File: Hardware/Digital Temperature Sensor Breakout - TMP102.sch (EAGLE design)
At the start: 12 parts, among them U1 TMP102-1:1

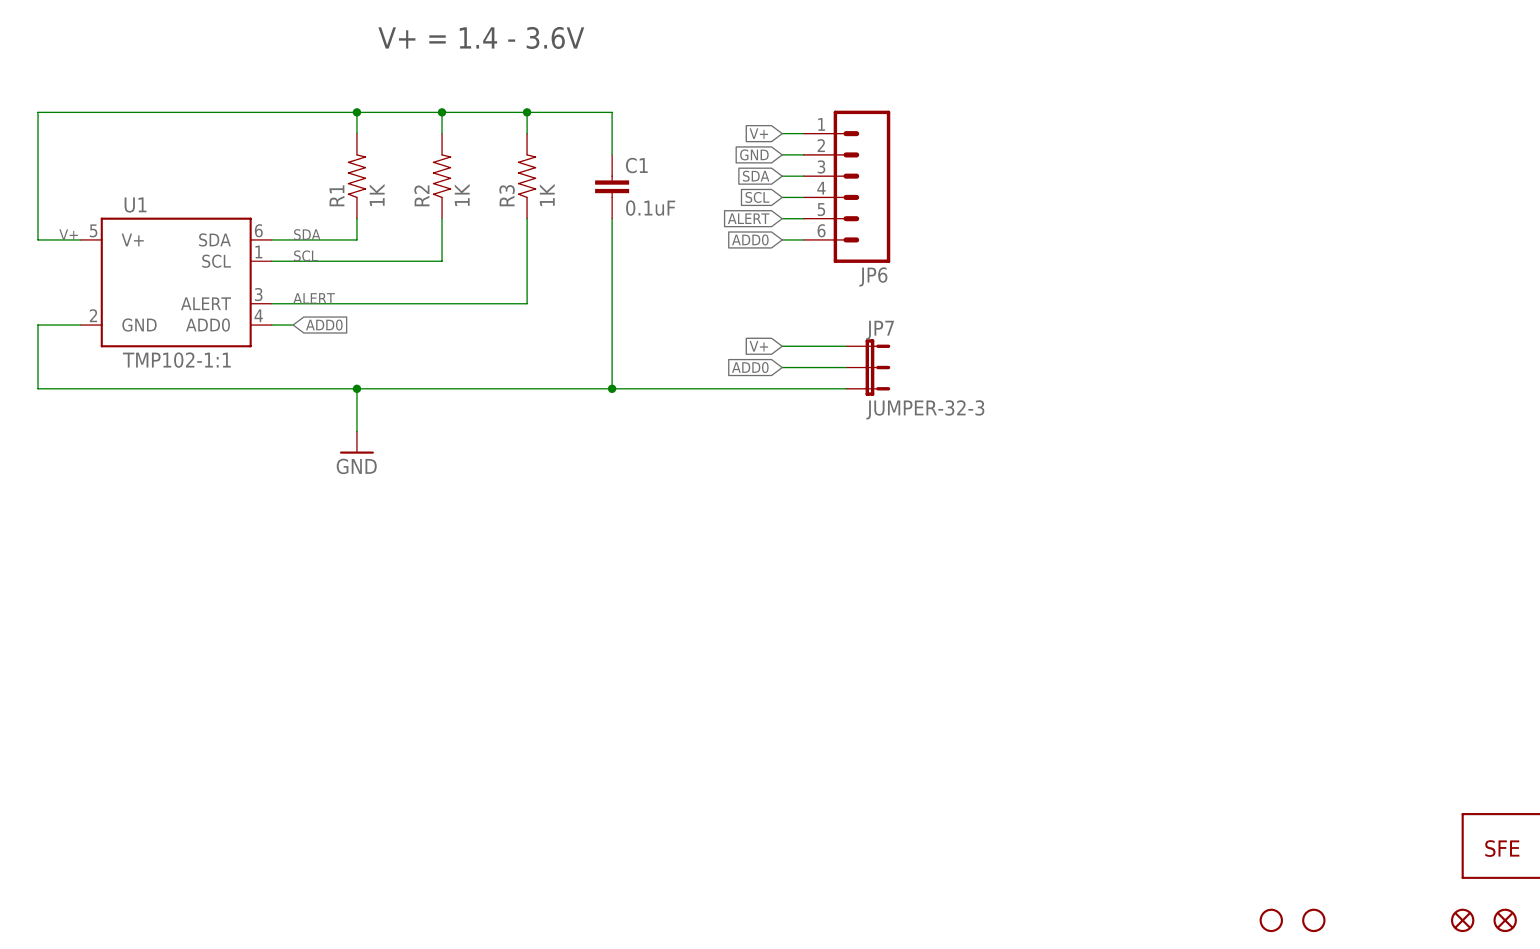
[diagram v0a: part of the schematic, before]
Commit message: Renamed board files
Renamed board files to match name of product on storefront. Also,
replaced main IC device with properly named variant from updated library
on github.
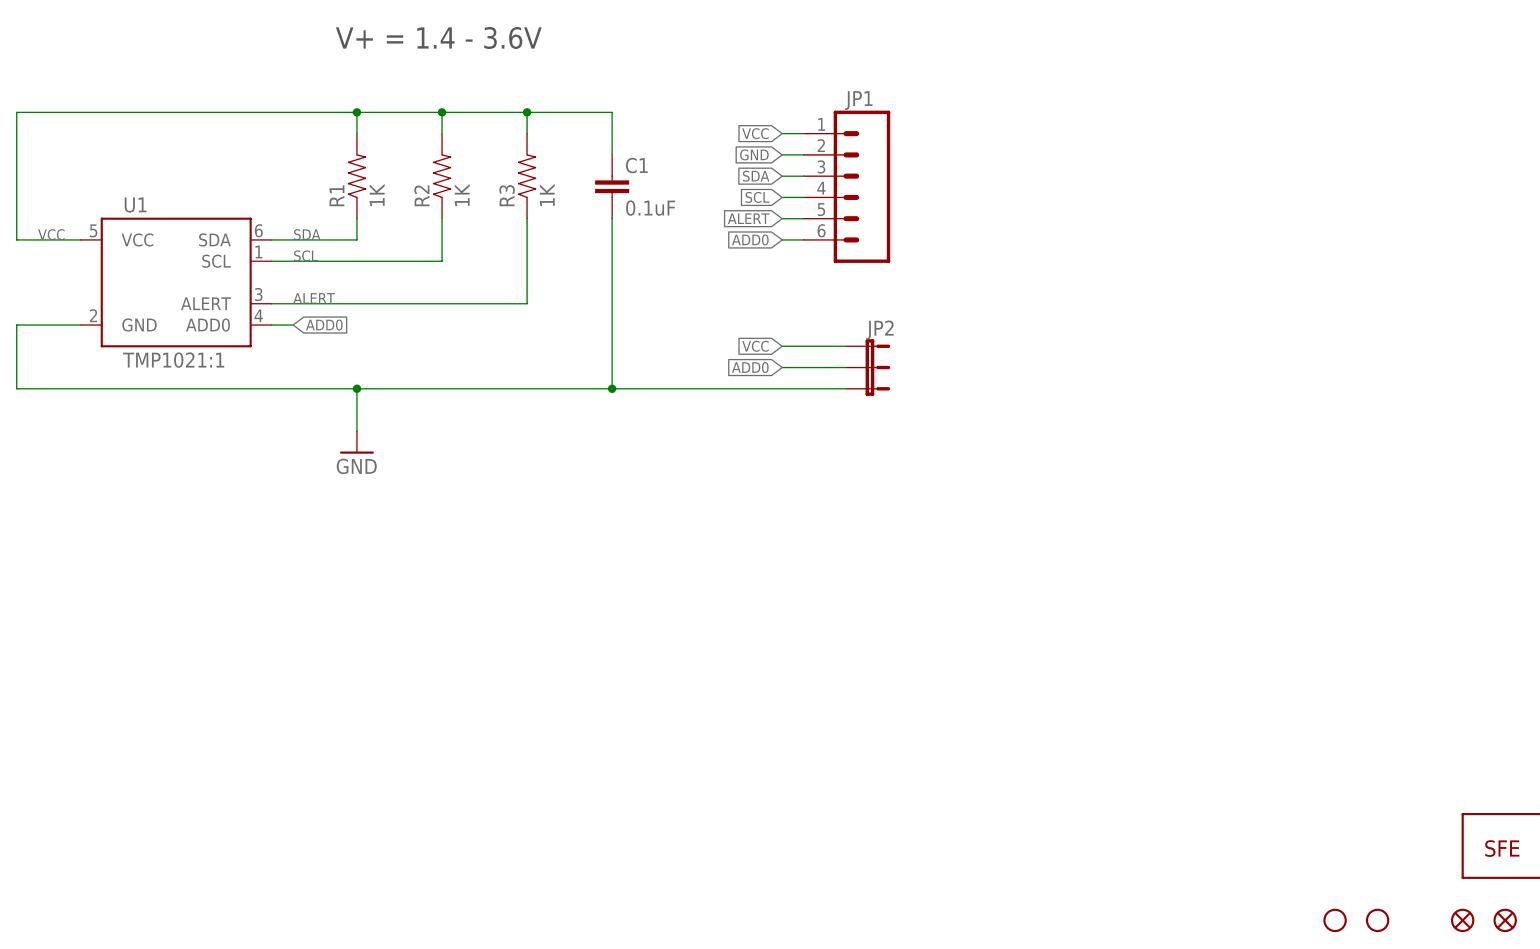
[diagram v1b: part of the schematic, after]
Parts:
- JP1: value STAND-OFFTIGHT -> (none); device SparkFun:STAND-OFFTIGHT -> SparkFun:M06SIP
- JP2: value STAND-OFFTIGHT -> JUMPER-32-3; device SparkFun:STAND-OFFTIGHT -> SparkFun:JUMPER-32-3
- JP6: value (none) -> STAND-OFFTIGHT; device SparkFun:M06SIP -> SparkFun:STAND-OFFTIGHT
- JP7: value JUMPER-32-3 -> STAND-OFFTIGHT; device SparkFun:JUMPER-32-3 -> SparkFun:STAND-OFFTIGHT
- U1: value TMP102-1:1 -> TMP1021:1; device SparkFun:TMP102-1:1 -> SparkFun-Sensors:TMP1021:1
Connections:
- removed net V+: C1.1, JP6.1, JP7.1, R1.2, R2.2, R3.2, U1.V+
- new net VCC: C1.1, JP1.1, JP2.1, R1.2, R2.2, R3.2, U1.VCC
- net ADD0: now also JP1.6, JP2.2; no longer JP6.6, JP7.2
- net ALERT: now also JP1.5; no longer JP6.5
- net GND: now also JP1.2, JP2.3; no longer JP6.2, JP7.3
- net SCL: now also JP1.4; no longer JP6.4
- net SDA: now also JP1.3; no longer JP6.3

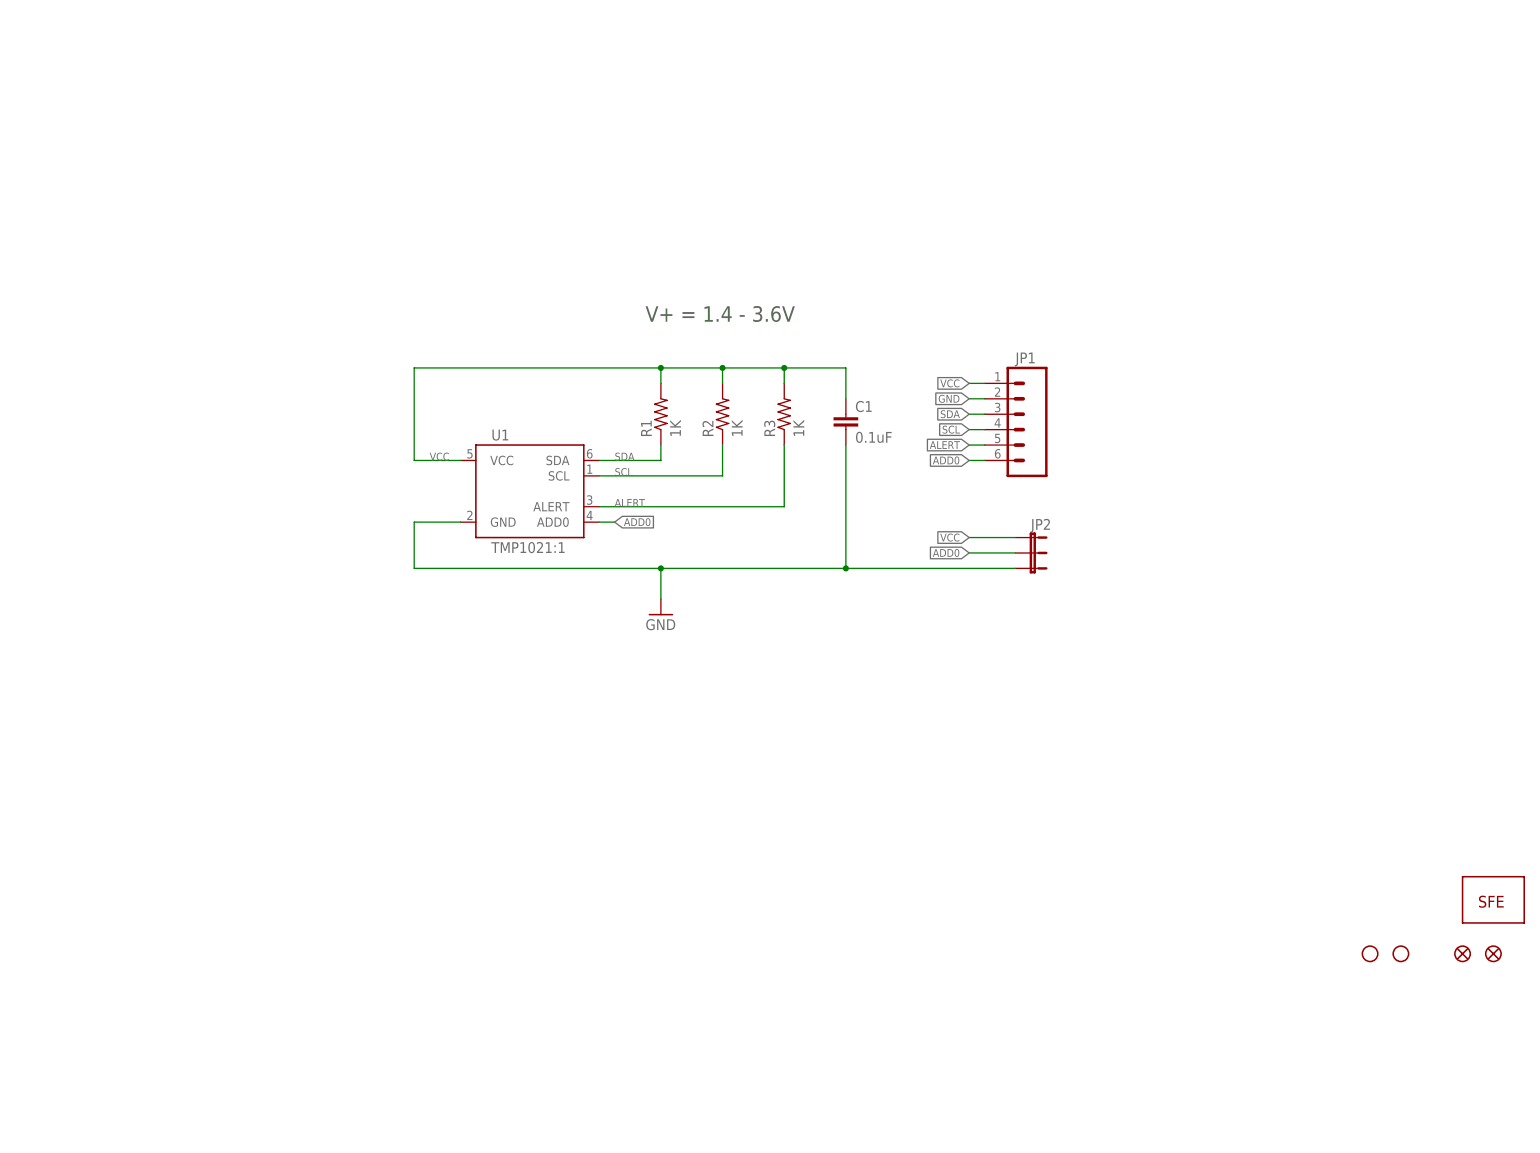
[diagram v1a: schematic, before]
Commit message: Added better info in schematic
Added a change log, version number, default i2c address info, and
creative commons note to schematic.
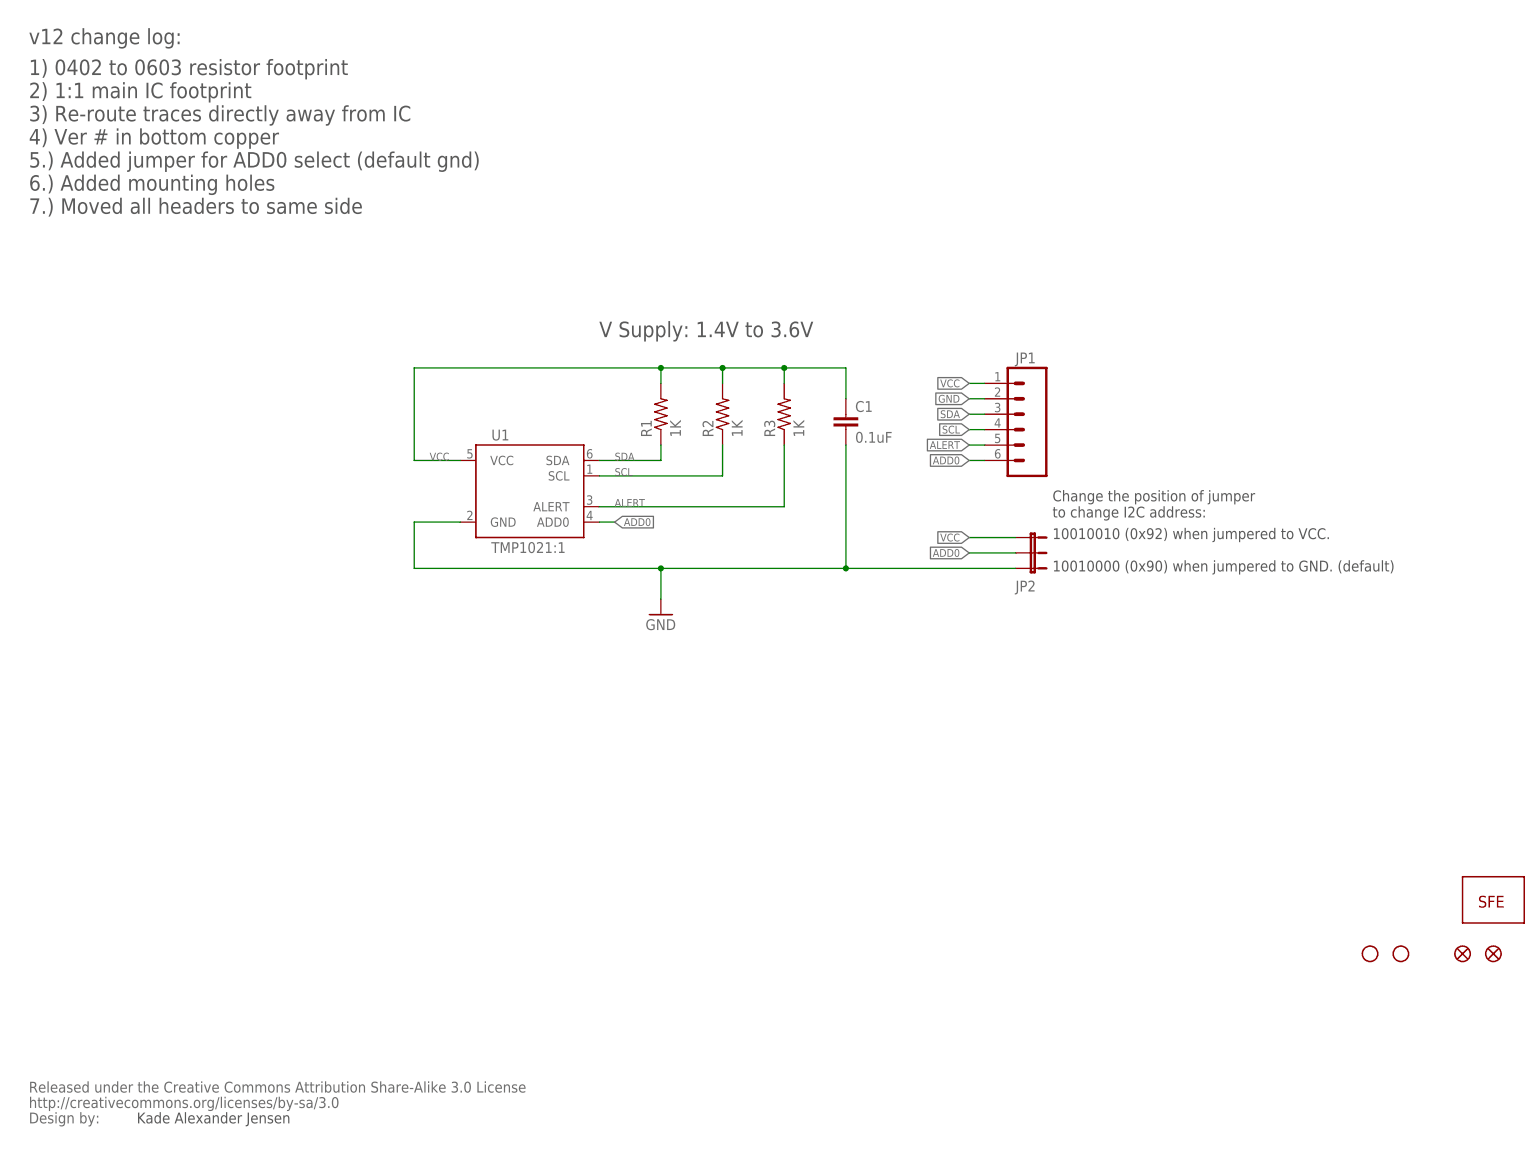
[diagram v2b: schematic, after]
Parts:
- added U$2: CREATIVE_COMMONS, SparkFun:CREATIVE_COMMONS
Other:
- note added: "1) 0402 to 0603 resistor footprint 2) 1:1 main IC footprint 3) Re-route traces directly away from IC 4) Ver # in bottom copper 5.) Added jumper for ADD0 select (default gnd) 6.) Added mounting holes 7.) Moved all headers to same side"
- note added: "10010010 (0x92) when jumpered to VCC. 10010000 (0x90) when jumpered to GND. (default)"
- note added: "Change the position of jumper to change I2C address:"
- note added: "Kade Alexander Jensen"
- note added: "V Supply: 1.4V to 3.6V"
- note added: "v12 change log:"
- note removed: "V+ = 1.4 - 3.6V"
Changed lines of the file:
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@@
 </classes>
 <parts>
-<part name="FRAME1" library="SparkFun" deviceset="FRAME-LETTER" device=""/>
 <part name="R1" library="SparkFun" deviceset="RESISTOR" device="0603-RES" value="1K"/>
 <part name="R2" library="SparkFun" deviceset="RESISTOR" device="0603-RES" value="1K"/>
@@
 <part name="JP6" library="SparkFun" deviceset="STAND-OFF" device="TIGHT"/>
 <part name="JP7" library="SparkFun" deviceset="STAND-OFF" device="TIGHT"/>
+<part name="FRAME1" library="SparkFun" deviceset="FRAME-LETTER" device=""/>
+<part name="U$2" library="SparkFun" deviceset="CREATIVE_COMMONS" device=""/>
 </parts>
 <sheets>
 <sheet>
 <plain>
-<text x="104.14" y="134.62" size="2.54" layer="97">V+ = 1.4 - 3.6V</text>
+<text x="96.52" y="132.08" size="2.54" layer="97">V Supply: 1.4V to 3.6V</text>
+<text x="20.32" y="2.54" size="1.778" layer="97">Kade Alexander Jensen</text>
+<text x="171.196" y="102.362" size="1.778" layer="97">Change the position of jumper
+to change I2C address:</text>
+<text x="171.196" y="93.472" size="1.778" layer="97">10010010 (0x92) when jumpered to VCC.
+10010000 (0x90) when jumpered to GND. (default)</text>
+<text x="2.54" y="180.34" size="2.54" layer="97">v12 change log:</text>
+<text x="2.54" y="152.4" size="2.54" layer="97">1) 0402 to 0603 resistor footprint
+2) 1:1 main IC footprint
+3) Re-route traces directly away from IC
+4) Ver # in bottom copper
+5.) Added jumper for ADD0 select (default gnd)
+6.) Added mounting holes
+7.) Moved all headers to same side</text>
 </plain>
 <instances>
-<instance part="FRAME1" gate="G$1" x="0" y="0"/>
-<instance part="FRAME1" gate="G$2" x="147.32" y="0"/>
 <instance part="R1" gate="G$1" x="106.68" y="119.38" rot="R90"/>
 <instance part="R2" gate="G$1" x="116.84" y="119.38" rot="R90"/>
@@
 </instance>
 <instance part="JP2" gate="G$1" x="167.64" y="99.06" smashed="yes" rot="R270">
-<attribute name="NAME" x="167.64" y="100.33" size="1.778" layer="95"/>
+<attribute name="NAME" x="165.1" y="90.17" size="1.778" layer="95"/>
 </instance>
 <instance part="U1" gate="G$1" x="86.36" y="106.68"/>
@@
 <instance part="JP6" gate="G$1" x="228.6" y="30.48"/>
 <instance part="JP7" gate="G$1" x="223.52" y="30.48"/>
+<instance part="FRAME1" gate="G$1" x="0" y="0"/>
+<instance part="FRAME1" gate="G$2" x="147.32" y="0"/>
+<instance part="U$2" gate="G$1" x="2.54" y="2.54"/>
 </instances>
 <busses>
@@
 </schematic>
 </drawing>
+<compatibility>
+<note version="6.3" minversion="6.2.2" severity="warning">
+Since Version 6.2.2 text objects can contain more than one line,
+which will not be processed correctly with this version.
+</note>
+</compatibility>
 </eagle>
